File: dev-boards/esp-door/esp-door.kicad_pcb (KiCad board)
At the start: 2 copper layers, 34 x 132 mm, 34 parts, among them J1 Conn_01x06, J2 Conn_01x03, J3 Conn_01x02, J4 Conn_01x03, J5 Conn_01x04, J6 Conn_01x02, Q1 BSS138, Q2 BSS84, Q3 BSS138, Q4 BSS84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

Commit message: WIP: Continue esp-door
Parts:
- removed the REF** at (135.1, 159.1)
- removed the REF** at (162.1, 159.1)
- added G***: LOGO, graphics:icon-speaker-4mm, B.Cu at (233.2, 156.0)
- added G***: LOGO, graphics:icon-bell-2mm, B.Cu at (226.0, 27.2)
- added LED2: LED, custom:LED_0805_2012Metric_Pad1.15x1.40mm_HandSolder_simple, F.Cu at (226.0, 30.0)
- added R2: 330R, Resistor_SMD:R_0805_2012Metric_Pad1.20x1.40mm_HandSolder, B.Cu at (226.0, 30.0)
- added REF**: MountingHole_3.2mm_M3, MountingHole:MountingHole_3.2mm_M3, F.Cu at (232.0, 148.0)
- added REF**: MountingHole_3.2mm_M3, MountingHole:MountingHole_3.2mm_M3, F.Cu at (216.0, 148.0)
- R1: moved to B.Cu
- moved R1 149.1 mm to (222.0, 30.0), turned to 180 degrees
- moved LED1 136.9 mm to (222.0, 30.0), turned to 0 degrees
- moved REF** 97.3 mm to (232.0, 30.0)
- moved Q1 89.8 mm to (216.2, 94.0)
- moved Q2 89.8 mm to (216.2, 98.1)
- moved Q3 89.8 mm to (224.0, 94.0)
- moved Q4 89.8 mm to (224.0, 98.1)
- moved Q5 89.8 mm to (231.8, 94.0)
- moved Q6 89.8 mm to (231.8, 98.1)
- moved RN1 89.8 mm to (220.1, 97.7)
- moved RN2 89.8 mm to (227.9, 97.7)
- moved RN3 89.8 mm to (227.9, 94.4)
- moved U1 89.8 mm to (222.8, 96.1)
- moved LS1 89.1 mm to (232.0, 152.8), turned to 0 degrees
- moved J6 88.1 mm to (231.0, 22.0)
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- renumbered R2 to R3
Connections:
- net LED_STATUS renamed C3_LED_STATUS
- U3 pad 13: unconnected-(U3-IO13-Pad13) -> CAM_LED_STATUS
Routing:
- net DOORBELL_RELAY: track 133.5 -> 0.00 mm, vias 1 -> 0
- net GPIO6: track 85.4 -> 0.00 mm, vias 3 -> 0
- net UART_1_RX: track 74.9 -> 0.00 mm, vias 1 -> 0
- net UART_1_TX: track 72.7 -> 0.00 mm, vias 1 -> 0
- net GPIO4: track 43.0 -> 0.00 mm
- net Net-(U2-SPK1): track 29.9 -> 0.00 mm, vias 1 -> 0
- net NEOPIXELS: track 29.8 -> 0.00 mm, vias 1 -> 0
- net Net-(U2-SPK2): track 29.3 -> 0.00 mm
- net UART_2_TX: track 25.8 -> 0.00 mm
- net +5V: track 39.4 -> 15.7 mm, vias 2 -> 0
- net UART_2_RX: track 18.0 -> 0.00 mm, vias 1 -> 0
- net Net-(RN3D-R4.1): track 16.0 -> 0.00 mm, vias 1 -> 0
- net BUTTON: track 15.0 -> 0.00 mm
- net Net-(LED1-A): track 13.2 -> 0.00 mm
- net BUTTON_LED_B: track 12.7 -> 0.00 mm
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- removed copper zone on F.Cu, net +5V
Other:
- board size 34 x 132 mm -> 28 x 144 mm
- board text added: "BTN"
- board text removed: "BELL"
- board text removed: "BT"
- board text removed: "SPEAKER"

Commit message: WIP: Rework esp-door PCB
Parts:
- added G***: LOGO, graphics:icon-bell-2mm, F.Cu at (226.0, 27.2)
- added REF**: OSHW-Logo_5.7x6mm_SilkScreen, Symbol:OSHW-Logo_5.7x6mm_SilkScreen, F.Cu at (224.0, 148.0)
- added REF**: OSHW-Logo_11.4x12mm_SilkScreen, Symbol:OSHW-Logo_11.4x12mm_SilkScreen, B.Cu at (224.0, 59.0)
- moved G*** 18.5 mm to (214.8, 155.9)
- moved LS1 18.5 mm to (213.5, 152.8)
- moved J1 8.50 mm to (222.0, 152.8)
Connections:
- RN1 pad 3: unconnected-(RN1C-R3.1-Pad3) -> GND
- RN1 pad 4: unconnected-(RN1D-R4.1-Pad4) -> GND
- RN1 pad 5: unconnected-(RN1D-R4.2-Pad5) -> GND
- RN1 pad 6: unconnected-(RN1C-R3.2-Pad6) -> GND
- RN3 pad 4: Net-(RN3D-R4.1) -> UART_2_RX
- RN3 pad 5: UART_2_RX -> Net-(RN3D-R4.2)
- U2 pad 3: Net-(RN3D-R4.1) -> Net-(RN3D-R4.2)
- U3 pad 13: CAM_LED_STATUS -> unconnected-(U3-IO13-Pad13)
- U3 pad 16: unconnected-(U3-IO16-Pad16) -> CAM_LED_STATUS
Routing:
- net GPIO4: track 0.00 -> 87.1 mm, vias 0 -> 1
- net DOORBELL_RELAY: track 0.00 -> 85.8 mm
- net C3_LED_STATUS: track 0.00 -> 80.1 mm
- net BUTTON_LED_R: track 0.00 -> 79.3 mm
- net GPIO6: track 0.00 -> 71.8 mm
- net BUTTON_LED_G: track 0.00 -> 70.3 mm
- net BUTTON: track 0.00 -> 68.0 mm, vias 0 -> 1
- net BUTTON_LED_B: track 0.00 -> 61.2 mm
- net Net-(RN3D-R4.2): track 0.00 -> 45.1 mm, vias 0 -> 1
- net UART_2_TX: track 0.00 -> 30.9 mm
- net +5V: track 15.7 -> 35.0 mm, vias 0 -> 2
- net Net-(U2-SPK1): track 0.00 -> 16.9 mm
- net CAM_LED_STATUS: track 0.00 -> 16.5 mm
- net UART_1_RX: track 0.00 -> 16.2 mm
- net UART_1_TX: track 0.00 -> 15.8 mm
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- added copper zone on F.Cu, net +5V
- added copper zone on B.Cu, net LD_OUT_JP
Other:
- board text added: "Button with RGB LED"
- board text added: "C3"
- board text added: "CAM"
- board text added: "DATA"
- board text added: "ESP32"
- board text added: "ESP32-C3 ESP32-CAM LD2410C DFPlayer Mini"
- board text added: "M3 mount holes 118x16mm spacing"
- board text added: "Modules"
- board text added: "Wifi Doorbell"
- board text added: "github.com/smkent/pcb 2024"
- board text added: "with presence sense, audio response"

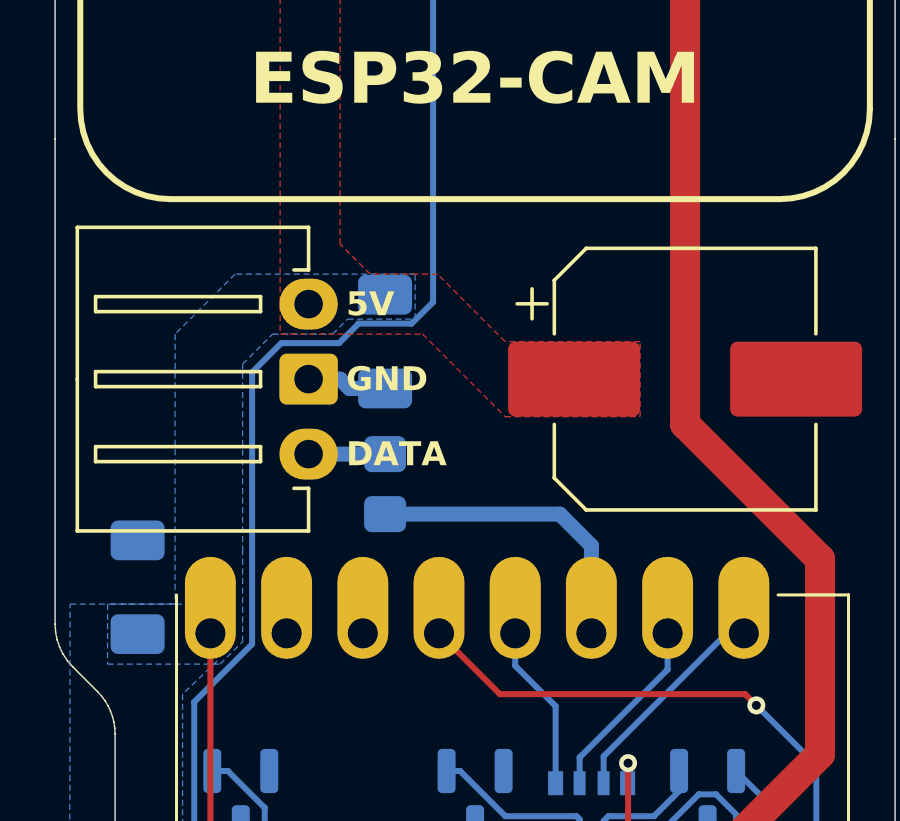
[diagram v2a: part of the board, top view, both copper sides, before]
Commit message: Swap Neopixel data and ground lines
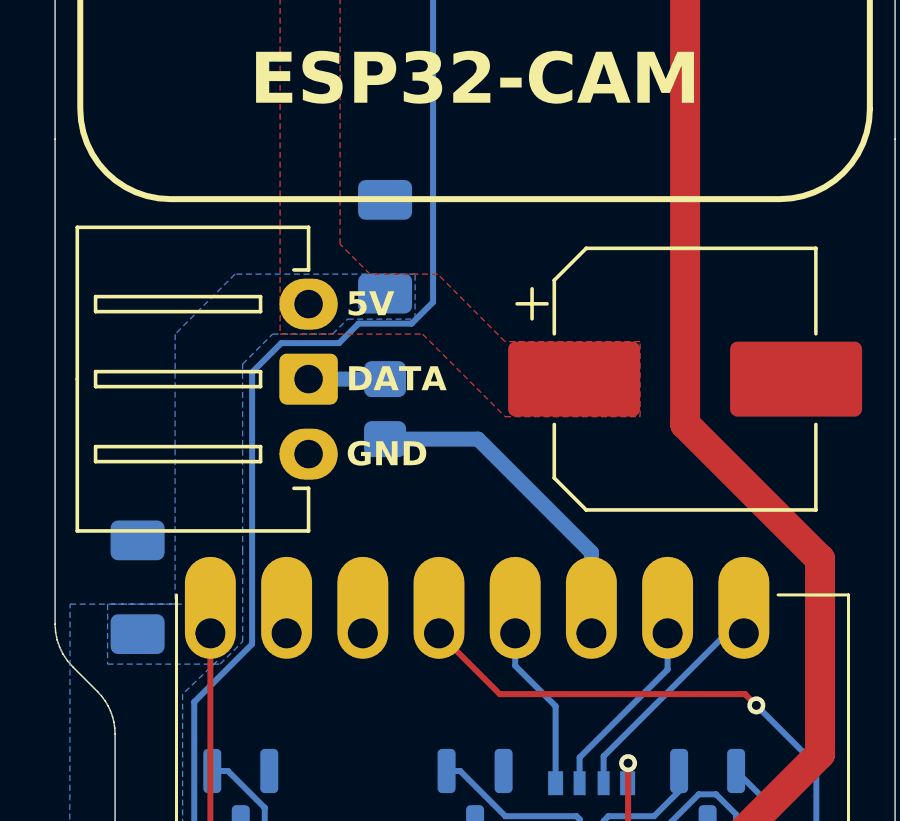
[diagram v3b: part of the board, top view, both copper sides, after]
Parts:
- moved C6 3.16 mm to (221.0, 75.6), turned to 90 degrees
- moved R3 2.50 mm to (221.0, 81.0)
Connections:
- J4 pad 2: GND -> Net-(J4-Pin_2)
- J4 pad 3: Net-(J4-Pin_3) -> GND
- R3 pad 2: Net-(J4-Pin_3) -> Net-(J4-Pin_2)
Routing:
- net GND: track 14.7 -> 12.1 mm
- net Net-(J4-Pin_3): track 2.55 -> 0.00 mm
- net Net-(J4-Pin_2): track 0.00 -> 2.55 mm
- net NEOPIXELS: track 10.2 -> 11.1 mm
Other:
- board text removed: "NEOPIXEL DATA"
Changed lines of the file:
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@@
 	(net 49 "LD_OUT_JP")
 	(net 50 "+5V")
-	(net 51 "Net-(J4-Pin_3)")
+	(net 51 "Net-(J4-Pin_2)")
 	(net 52 "CAM_LED_STATUS")
 	(net 53 "Net-(RN3D-R4.2)")
@@
 		(tags "capacitor electrolytic")
 		(property "Reference" "C1"
-			(at 0 -5.3 360)
+			(at 0 -5.3 0)
 			(layer "F.SilkS")
 			(hide yes)
@@
 		)
 		(property "Value" "1000uF"
-			(at 0 5.3 360)
+			(at 0 5.3 0)
 			(layer "F.Fab")
 			(effects
@@
 		)
 		(fp_text user "${REFERENCE}"
-			(at 0 0 360)
+			(at 0 0 0)
 			(layer "F.Fab")
 			(effects
@@
 		(tags "connector JST XH horizontal")
 		(property "Reference" "LS1"
-			(at 1.25 -2 360)
+			(at 1.25 -2 0)
 			(layer "F.SilkS")
 			(hide yes)
@@
 		)
 		(property "Value" "Speaker"
-			(at 1.25 8.8 360)
+			(at 1.25 8.8 0)
 			(layer "F.Fab")
 			(effects
@@
 		)
 		(fp_text user "${REFERENCE}"
-			(at 1.25 1.85 360)
+			(at 1.25 1.85 0)
 			(layer "F.Fab")
 			(effects
@@
 		(tags "LED handsolder")
 		(property "Reference" "LED2"
-			(at 0 -1.65 360)
+			(at 0 -1.65 0)
 			(layer "F.SilkS")
 			(hide yes)
@@
 		)
 		(property "Value" "LED"
-			(at 0 1.65 360)
+			(at 0 1.65 0)
 			(layer "F.Fab")
 			(effects
@@
 		)
 		(fp_text user "${REFERENCE}"
-			(at 0 0 360)
+			(at 0 0 0)
 			(layer "F.Fab")
 			(effects
@@
 		(at 224 134.11)
 		(property "Reference" "U2"
-			(at 0 -11.235 360)
+			(at 0 -11.235 0)
 			(layer "F.SilkS")
 			(hide yes)
@@
 		)
 		(property "Value" "DFR0299"
-			(at -1.51 11.065 360)
+			(at -1.51 11.065 0)
 			(layer "F.Fab")
 			(effects
@@
 		)
 		(property "Footprint" "aliexpress:DFPlayer-Mini-DFR0299-module"
-			(at 0 0 360)
+			(at 0 0 0)
 			(layer "F.Fab")
 			(hide yes)
@@
 		)
 		(property "Datasheet" ""
-			(at 0 0 360)
+			(at 0 0 0)
 			(layer "F.Fab")
 			(hide yes)
@@
 		)
 		(property "Description" "Dfplayer - a Mini Mp3 Player"
-			(at 0 0 360)
+			(at 0 0 0)
 			(layer "F.Fab")
 			(hide yes)
@@
 			(remove_unused_layers no)
 			(roundrect_rratio 0.1470588235)
-			(net 2 "GND")
+			(net 51 "Net-(J4-Pin_2)")
 			(pinfunction "Pin_2")
 			(pintype "passive")
@@
 			(layers "*.Cu" "*.Mask")
 			(remove_unused_layers no)
-			(net 51 "Net-(J4-Pin_3)")
+			(net 2 "GND")
 			(pinfunction "Pin_3")
 			(pintype "passive")
@@
 		(tags "LED handsolder")
 		(property "Reference" "LED1"
-			(at 0 -1.65 360)
+			(at 0 -1.65 0)
 			(layer "F.SilkS")
 			(hide yes)
@@
 		)
 		(property "Value" "LED"
-			(at 0 1.65 360)
+			(at 0 1.65 0)
 			(layer "F.Fab")
 			(effects
@@
 		)
 		(fp_text user "${REFERENCE}"
-			(at 0 0 360)
+			(at 0 0 0)
 			(layer "F.Fab")
 			(effects
@@
 	(footprint "Resistor_SMD:R_0805_2012Metric_Pad1.20x1.40mm_HandSolder"
 		(layer "B.Cu")
-		(at 221 83.5 90)
+		(at 221 81 90)
 		(descr "Resistor SMD 0805 (2012 Metric), square (rectangular) end terminal, IPC_7351 nominal with elongated pad for handsoldering. (Body size source: IPC-SM-782 page 72, https://www.pcb-3d.com/wordpress/wp-content/uploads/ipc-sm-782a_amendment_1_and_2.pdf), generated with kicad-footprint-generator")
 		(tags "resistor handsolder")
@@
 			(layers "B.Cu" "B.Paste" "B.Mask")
 			(roundrect_rratio 0.208333)
-			(net 51 "Net-(J4-Pin_3)")
+			(net 51 "Net-(J4-Pin_2)")
 			(pintype "passive")
 		)
@@
 	(footprint "custom:C_1206_3216Metric_Pad1.33x1.80mm_HandSolder"
 		(layer "B.Cu")
-		(at 221 78.75 -90)
+		(at 221 75.5875 90)
 		(descr "Capacitor SMD 1206 (3216 Metric), square (rectangular) end terminal, IPC_7351 nominal with elongated pad for handsoldering. (Body size source: IPC-SM-782 page 76, https://www.pcb-3d.com/wordpress/wp-content/uploads/ipc-sm-782a_amendment_1_and_2.pdf), generated with kicad-footprint-generator")
 		(tags "capacitor handsolder")
@@
 		)
 		(property "Footprint" "custom:C_1206_3216Metric_Pad1.33x1.80mm_HandSolder"
-			(at 0 0 90)
+			(at 0 0 -90)
 			(unlocked yes)
 			(layer "B.Fab")
@@
 		)
 		(property "Datasheet" ""
-			(at 0 0 90)
+			(at 0 0 -90)
 			(unlocked yes)
 			(layer "B.Fab")
@@
 		)
 		(property "Description" "Unpolarized capacitor, small symbol"
-			(at 0 0 90)
+			(at 0 0 -90)
 			(unlocked yes)
 			(layer "B.Fab")
@@
 		(attr smd)
 		(fp_line
-			(start 0.2 0.4)
-			(end 0.2 -0.4)
+			(start -0.2 -0.4)
+			(end -0.2 0.4)
 			(stroke
 				(width 0.1)
@@
 		)
 		(fp_line
-			(start -0.6 0)
-			(end -0.2 0)
+			(start 0.6 0)
+			(end 0.2 0)
 			(stroke
 				(width 0.1)
@@
 		)
 		(fp_line
-			(start 0.6 0)
-			(end 0.2 0)
+			(start -0.6 0)
+			(end -0.2 0)
 			(stroke
 				(width 0.1)
@@
 		)
 		(fp_line
-			(start -0.2 -0.4)
-			(end -0.2 0.4)
+			(start 0.2 0.4)
+			(end 0.2 -0.4)
 			(stroke
 				(width 0.1)
@@
 		)
 		(fp_line
-			(start -2.48 1.15)
-			(end -2.48 -1.15)
+			(start 2.48 -1.15)
+			(end 2.48 1.15)
 			(stroke
 				(width 0.05)
@@
 		)
 		(fp_line
-			(start 2.48 1.15)
-			(end -2.48 1.15)
+			(start -2.48 -1.15)
+			(end 2.48 -1.15)
 			(stroke
 				(width 0.05)
@@
 		)
 		(fp_line
-			(start -2.48 -1.15)
-			(end 2.48 -1.15)
+			(start 2.48 1.15)
+			(end -2.48 1.15)
 			(stroke
 				(width 0.05)
@@
 		)
 		(fp_line
-			(start 2.48 -1.15)
-			(end 2.48 1.15)
+			(start -2.48 1.15)
+			(end -2.48 -1.15)
 			(stroke
 				(width 0.05)
@@
 		)
 		(fp_line
-			(start -1.6 0.8)
-			(end -1.6 -0.8)
+			(start 1.6 -0.8)
+			(end 1.6 0.8)
 			(stroke
 				(width 0.1)
@@
 		)
 		(fp_line
-			(start 1.6 0.8)
-			(end -1.6 0.8)
+			(start -1.6 -0.8)
+			(end 1.6 -0.8)
 			(stroke
 				(width 0.1)
@@
 		)
 		(fp_line
-			(start -1.6 -0.8)
-			(end 1.6 -0.8)
+			(start 1.6 0.8)
+			(end -1.6 0.8)
 			(stroke
 				(width 0.1)
@@
 		)
 		(fp_line
-			(start 1.6 -0.8)
-			(end 1.6 0.8)
+			(start -1.6 0.8)
+			(end -1.6 -0.8)
 			(stroke
 				(width 0.1)
@@
 		)
 		(pad "1" smd roundrect
-			(at -1.5625 0 270)
+			(at -1.5625 0 90)
 			(size 1.325 1.8)
 			(layers "B.Cu" "B.Paste" "B.Mask")
@@
 		)
 		(pad "2" smd roundrect
-			(at 1.5625 0 270)
+			(at 1.5625 0 90)
 			(size 1.325 1.8)
 			(layers "B.Cu" "B.Paste" "B.Mask")
@@
 	)
 	(gr_text "GND"
-		(at 217 80 0)
+		(at 217 82.5 0)
 		(layer "B.SilkS" knockout)
 		(effects
@@
 		)
 	)
-	(gr_text "NEOPIXEL\nDATA"
-		(at 217 82.5 0)
+	(gr_text "DATA"
+		(at 217 80 0)
 		(layer "B.SilkS" knockout)
 		(effects
@@
 	)
 	(gr_text "GND"
-		(at 219.7 80 0)
+		(at 219.7 82.5 0)
 		(layer "F.SilkS" knockout)
 		(effects
@@
 	)
 	(gr_text "DATA"
-		(at 219.7 82.5 0)
+		(at 219.7 80 0)
 		(layer "F.SilkS" knockout)
 		(effects
@@
 	)
 	(segment
-		(start 221 80.3125)
-		(end 219.8125 80.3125)
-		(width 0.5)
-		(layer "B.Cu")
-		(net 2)
-	)
-	(segment
 		(start 233.5 97.7675)
 		(end 233.5 93.861552)
@@
 	)
 	(segment
-		(start 219.5 80)
-		(end 218.45 80)
-		(width 0.5)
-		(layer "B.Cu")
-		(net 2)
-	)
-	(segment
 		(start 232.5655 98.5)
 		(end 232.7675 98.5)
@@
 	)
 	(segment
-		(start 219.8125 80.3125)
-		(end 219.5 80)
-		(width 0.5)
-		(layer "B.Cu")
-		(net 2)
-	)
-	(segment
 		(start 226.25 151.25)
 		(end 227.434314 151.25)
@@
 	)
 	(segment
-		(start 227.877448 85.551485)
-		(end 226.825963 84.5)
+		(start 224.1 82)
+		(end 221 82)
 		(width 0.5)
 		(layer "B.Cu")
@@
 	(segment
 		(start 227.877448 88.474)
-		(end 227.877448 85.551485)
+		(end 227.877448 85.777448)
 		(width 0.5)
 		(layer "B.Cu")
@@
 	)
 	(segment
-		(start 226.825963 84.5)
-		(end 221 84.5)
+		(start 227.877448 85.777448)
+		(end 224.1 82)
 		(width 0.5)
 		(layer "B.Cu")
@@
 	)
 	(segment
-		(start 221 82.5)
-		(end 218.45 82.5)
+		(start 218.45 80)
+		(end 221 80)
 		(width 0.5)
 		(layer "B.Cu")
@@
 			(pts
 				(xy 214.001167 78.5) (xy 214 87.5) (xy 211.75 87.5) (xy 211.75 89.5) (xy 215.5 89.5) (xy 216.251604 88.75)
-				(xy 216.251604 85.75) (xy 216.251604 85.75) (xy 216.250221 79.5) (xy 217.25 78.5) (xy 219.25 78.5)
-				(xy 219.75 78) (xy 222 78) (xy 222.001604 76.5) (xy 216 76.5)
+				(xy 216.251604 85.75) (xy 216.250221 79.5) (xy 217.25 78.5) (xy 219.25 78.5) (xy 219.75 78) (xy 222 78)
+				(xy 222.001604 76.5) (xy 216 76.5)
 			)
 		)

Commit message: Rotate DFPlayer Mini on PCB for easier microSD card access
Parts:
- moved C2 19.7 mm to (230.5, 141.8), turned to 90 degrees
- moved G*** 18.5 mm to (233.2, 155.9)
- moved LS1 18.5 mm to (232.0, 152.8)
- moved J1 8.53 mm to (213.5, 152.8)
- turned U2 to 180 degrees
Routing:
- net UART_2_TX: track 30.9 -> 50.4 mm, vias 0 -> 1
- net Net-(U2-SPK2): track 11.9 -> 29.3 mm
- net BUTTON: track 68.0 -> 84.0 mm
- net GPIO6: track 71.8 -> 87.6 mm
- net Net-(RN3D-R4.2): track 45.1 -> 58.3 mm, vias 1 -> 2
- net BUTTON_LED_B: track 61.2 -> 69.8 mm
- net BUTTON_LED_R: track 79.3 -> 87.8 mm
- net BUTTON_LED_G: track 70.3 -> 78.7 mm
- net Net-(U2-SPK1): track 16.9 -> 24.3 mm
- net UART_1_RX: track 16.2 -> 15.6 mm
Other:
- board text added: "M3 mounting holes 118x16mm spacing"
- board text removed: "M3 mount holes 118x16mm spacing"
